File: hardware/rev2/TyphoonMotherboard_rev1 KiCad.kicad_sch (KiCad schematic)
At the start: 45 parts, among them J1 Conn_02x04_Odd_Even, J2 Conn_01x04_Pin, J3 UJ20-C-H-C-4-SMT-TR, J5 Conn_01x02_Pin, J6 Conn_01x02_Pin, J7 Conn_01x04_Pin, SW1 SW_Push, SW2 SW_Push, SW3 SW_Push, U1 USBLC6-2SC6, U2 ESP32-S3-WROOM-1, U3 SN65HVD233, U4 TPS62130A, U5 TPS62130A

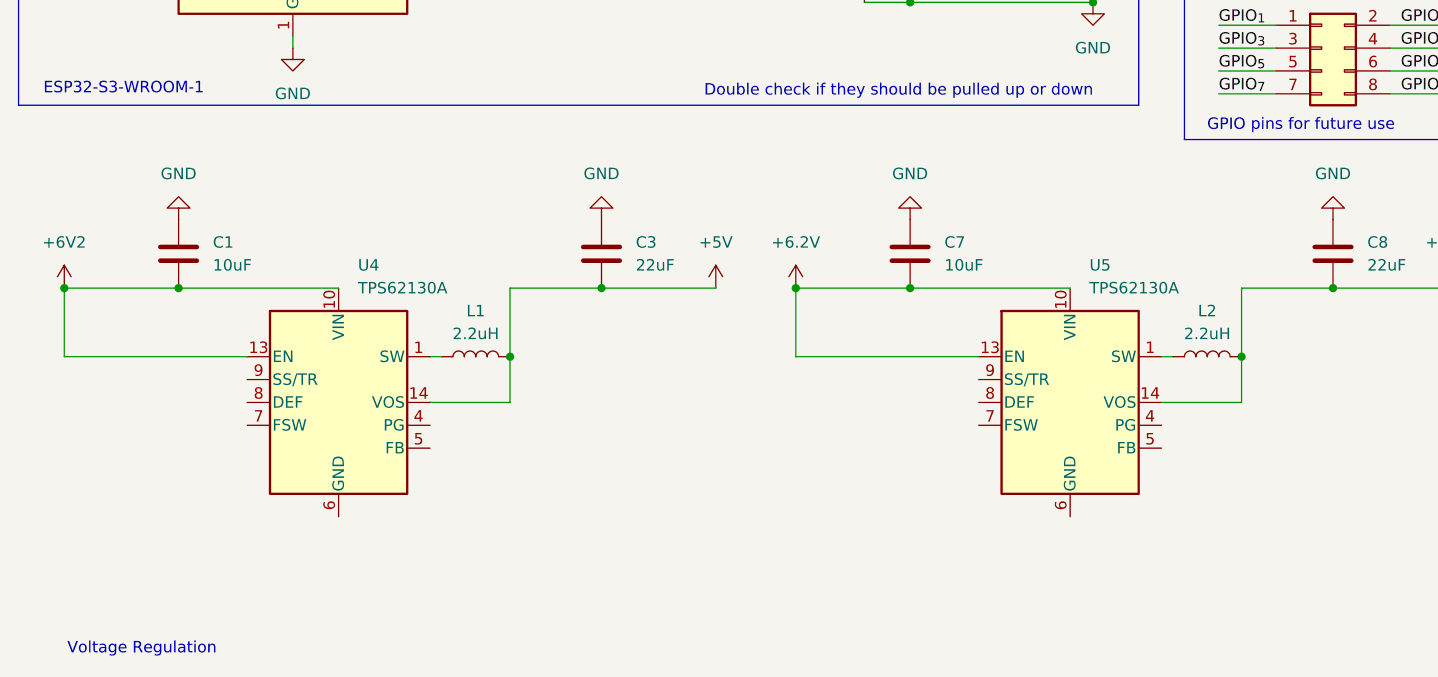
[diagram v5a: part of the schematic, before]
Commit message: Updated rev2 voltage regulation schematic (TP62133 regulator)
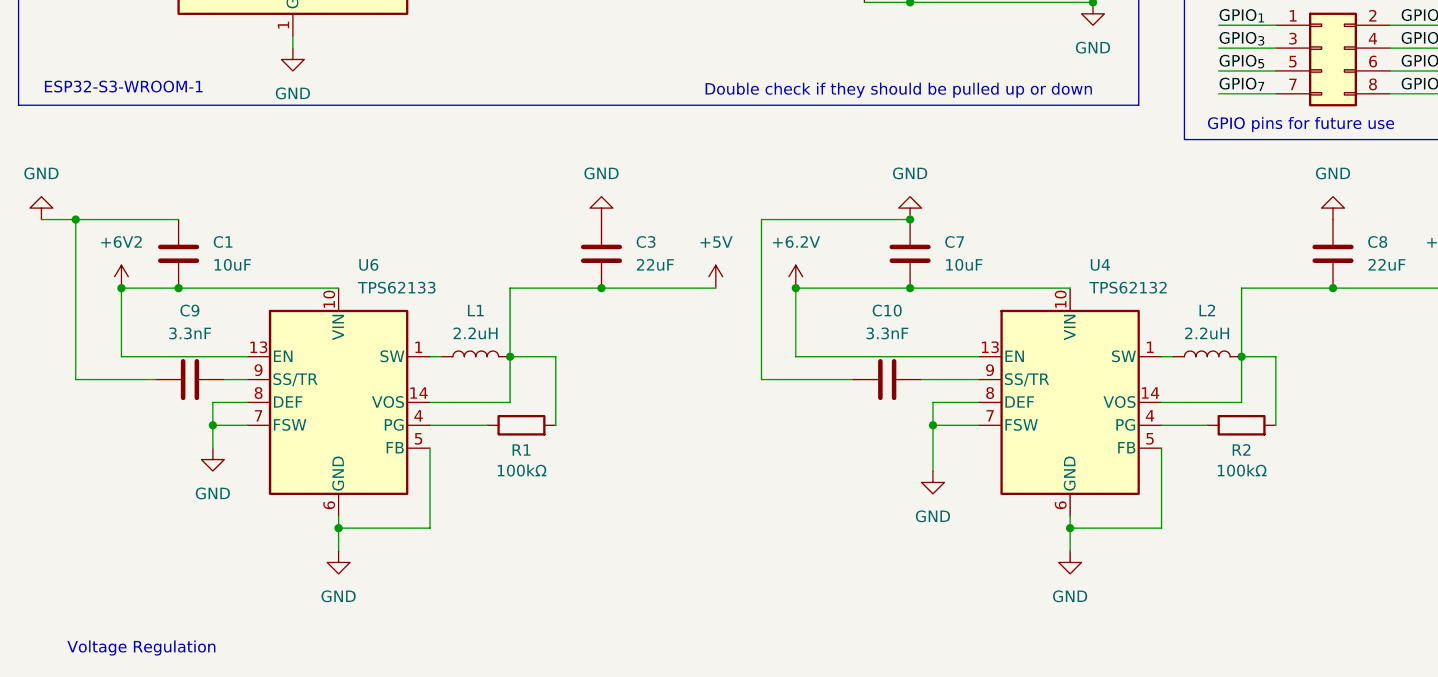
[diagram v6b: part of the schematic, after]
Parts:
- removed U4, U5: TPS62130A, Package_DFN_QFN:VQFN-16-1EP_3x3mm_P0.5mm_EP1.68x1.68mm_ThermalVias, symbol Regulator_Switching:TPS62130A
- added C10, C9: 3.3nF, symbol Device:C
- added R1, R2: 100kΩ, symbol Device:R
- added U4: TPS62132, Package_DFN_QFN:VQFN-16-1EP_3x3mm_P0.5mm_EP1.68x1.68mm_ThermalVias, symbol Regulator_Switching:TPS62132
- added U6: TPS62133, Package_DFN_QFN:VQFN-16-1EP_3x3mm_P0.5mm_EP1.68x1.68mm_ThermalVias, symbol Regulator_Switching:TPS62133
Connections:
- net +3V3: now also R2.2, U4.14 (VOS)
- net +5V: now also R1.2, U6.14 (VOS)
- net +6.2V: now also U4.10 (VIN), U4.11 (VIN), U4.12 (VIN), U4.13 (EN)
- net +6V2: now also U6.10 (VIN), U6.11 (VIN), U6.12 (VIN), U6.13 (EN)
- net GND: now also C10.1, C9.1, U4.15 (GND), U4.16 (GND), U4.17 (GND), U4.5 (FB), U4.6 (GND), U4.7 (FSW), U4.8 (DEF), U6.15 (GND), U6.16 (GND), U6.17 (GND), U6.5 (FB), U6.6 (GND), U6.7 (FSW), U6.8 (DEF)
- net at L1.1: now also U6.1 (SW), U6.2 (SW), U6.3 (SW)
- net at L2.1: now also U4.1 (SW), U4.2 (SW), U4.3 (SW)
- new net: R2.1, U4.4 (PG)
- new net: C10.2, U4.9 (SS/TR)
- new net: R1.1, U6.4 (PG)
- new net: C9.2, U6.9 (SS/TR)

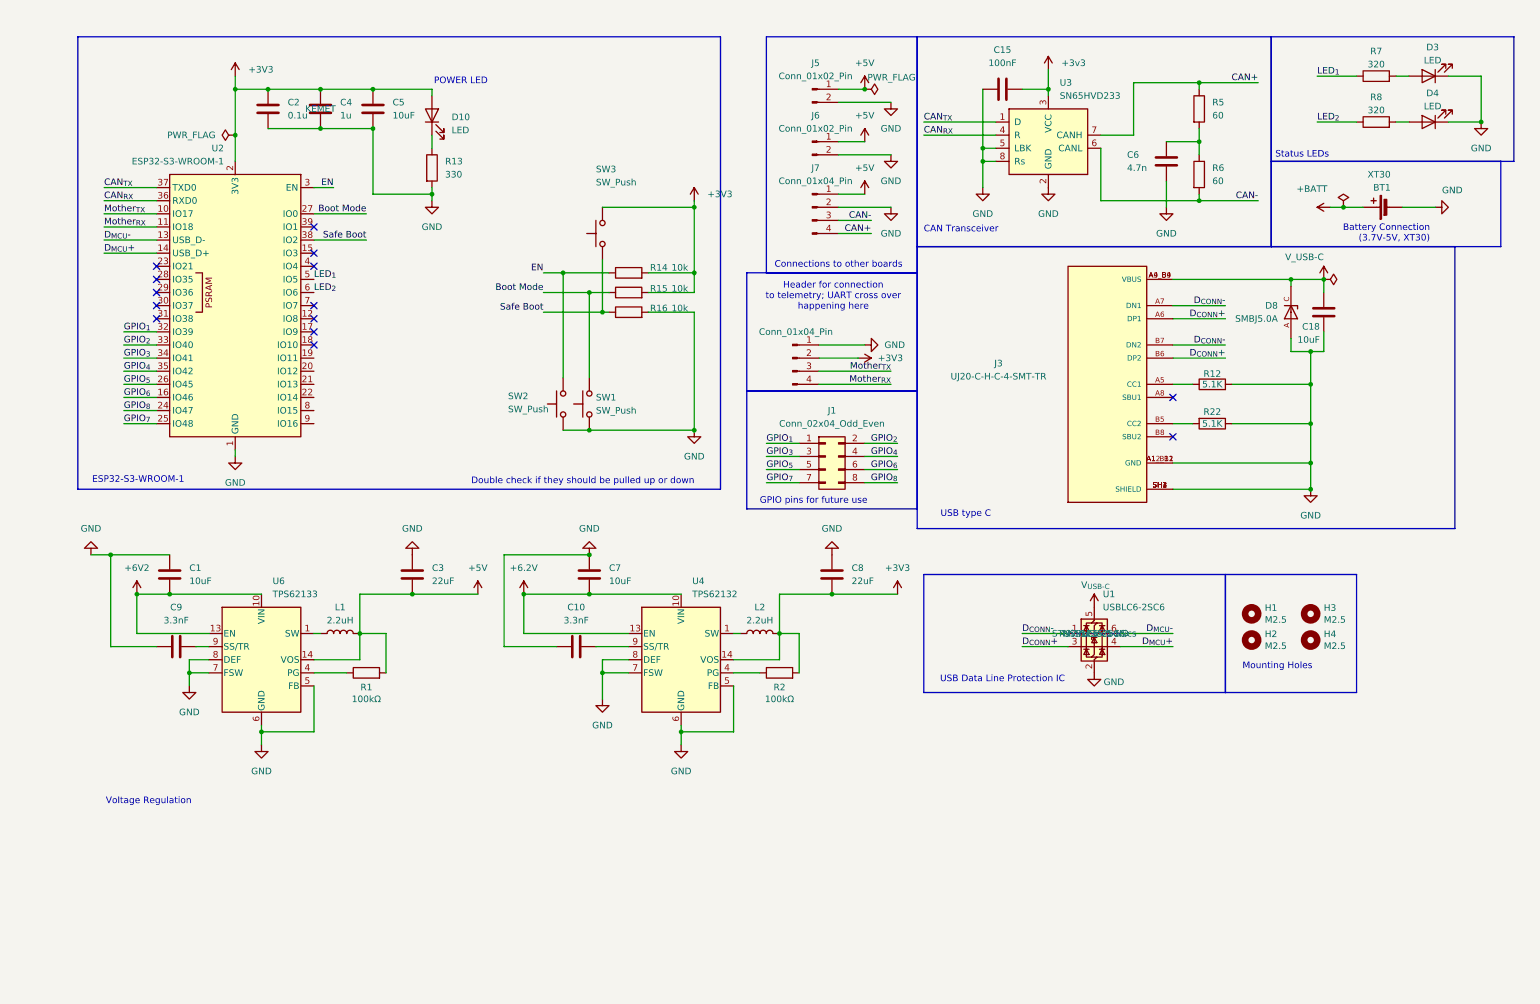
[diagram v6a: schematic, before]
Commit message: Finished Schematic Ready for PCB Design
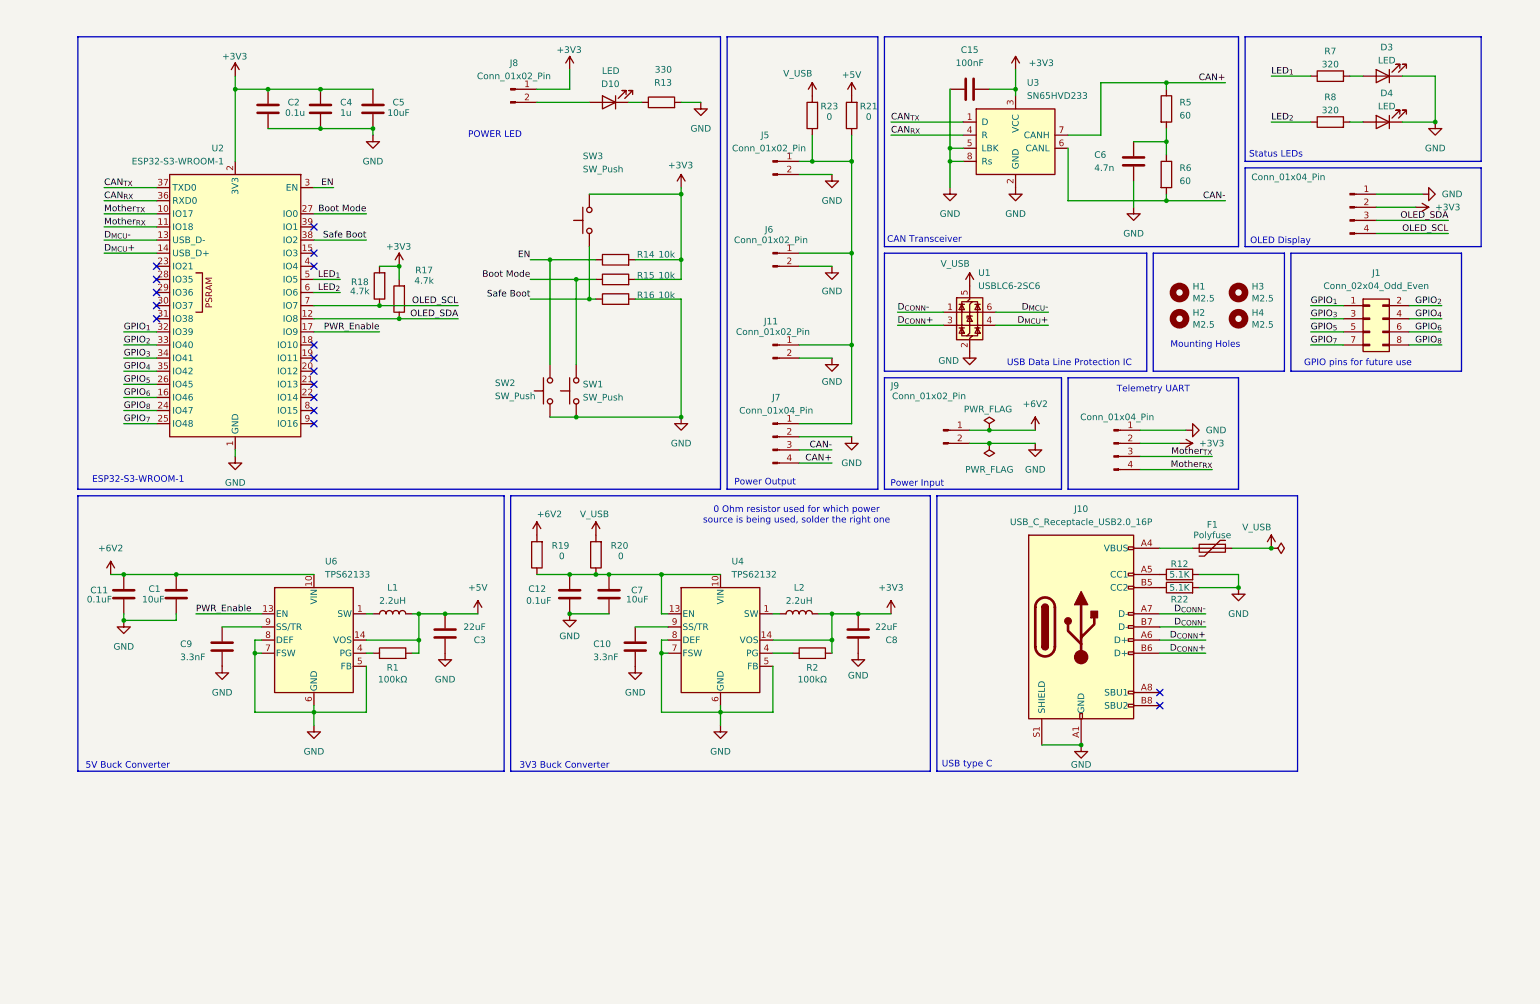
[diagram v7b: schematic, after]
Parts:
- removed BT1: XT30, Connector_AMASS:AMASS_XT30U-F_1x02_P5.0mm_Vertical, symbol Device:Battery_Cell
- removed C18: 10uF, Capacitor_SMD:C_0603_1608Metric, symbol Device:C
- removed D8: SMBJ5.0A, SMBJ5.0A:DIOM4336X265N, symbol SMBJ5.0A:SMBJ5.0A
- removed J3: UJ20-C-H-C-4-SMT-TR, UJ20-C-H-C-4-SMT-TR:CUI_UJ20-C-H-C-4-SMT-TR, symbol UJ20-C-H-C-4-SMT-TR:UJ20-C-H-C-4-SMT-TR
- added C11, C12: 0.1uF, Capacitor_SMD:C_0603_1608Metric, symbol Device:C
- added F1: Polyfuse, Fuse:Fuse_1206_3216Metric, symbol Device:Polyfuse
- added J10: USB_C_Receptacle_USB2.0_16P, Connector_USB:USB_C_Receptacle_JAE_DX07S016JA1R1500, symbol Connector:USB_C_Receptacle_USB2.0_16P
- added J11, J8, J9: Conn_01x02_Pin, Connector_JST:JST_XH_B2B-XH-A_1x02_P2.50mm_Vertical, symbol Connector:Conn_01x02_Pin
- added J4: Conn_01x04_Pin, Connector_JST:JST_XH_B4B-XH-A_1x04_P2.50mm_Vertical, symbol Connector:Conn_01x04_Pin
- added R17, R18: 4.7k, Resistor_SMD:R_0603_1608Metric, symbol Device:R
- added R19, R20, R21, R23: 0, Resistor_SMD:R_1206_3216Metric, symbol Device:R
- C1, C10, C3, C7, C8, C9: footprint (none) -> Capacitor_SMD:C_0603_1608Metric
- L1, L2: footprint (none) -> Inductor_SMD:L_0805_2012Metric
- R1, R2: footprint (none) -> Resistor_SMD:R_0603_1608Metric
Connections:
- net +3v3 is gone; now on net +3V3: C15.2, U3.3 (VCC)
- net +3V3: now also J4.2 (Pin_2), J8.1 (Pin_1), R17.2, R18.2; no longer D10.2 (A)
- net +5V: now also R21.2; no longer C3.2, J5.1 (Pin_1), J6.1 (Pin_1), J7.1 (Pin_1), L1.2, R1.2, U6.14 (VOS)
- net +6V2: now also C11.2, J9.1 (Pin_1), R19.2; no longer U6.13 (EN)
- net D_{CONN}+: now also J10.A6 (D+), J10.B6 (D+)
- net D_{CONN}-: now also J10.A7 (D-), J10.B7 (D-)
- net GND: now also R22.2, C11.1, C12.1, J10.A1 (GND), J10.A12 (GND), J10.B1 (GND), J10.B12 (GND), J10.S1 (SHIELD), J11.2 (Pin_2), J4.1 (Pin_1), J9.2 (Pin_2); no longer R22.1
- net at R12.1: now also J10.A5 (CC1)
- net OLED_SDA: now reaches U2.12 (IO8)
- net OLED_SDA: now also J4.3 (Pin_3), R17.1
- net PWR_Enable: now reaches U2.17 (IO9)
- net PWR_Enable: now also U6.13 (EN)
- net OLED_SCL: now reaches U2.7 (IO7)
- net OLED_SCL: now also J4.4 (Pin_4), R18.1
- net +6.2V: no longer names the net of C7.2, U4.10 (VIN), U4.11 (VIN), U4.12 (VIN), U4.13 (EN)
- net +6.2V: now also C12.2, R19.1, R20.1
- net V_{USB-C} renamed V_USB
- net V_USB: now also F1.1, R20.2, R23.2
- new net: D10.2 (A), J8.2 (Pin_2)
- new net: C3.2, L1.2, R1.2, U6.14 (VOS)
- new net: J10.B5 (CC2), R22.1
- new net: F1.2, J10.A4 (VBUS), J10.A9 (VBUS), J10.B4 (VBUS), J10.B9 (VBUS)
- new net: J11.1 (Pin_1), J5.1 (Pin_1), J6.1 (Pin_1), J7.1 (Pin_1), R21.1, R23.1
- no-connect marks 14 -> 17
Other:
- note added: "0 Ohm resistor used for which power source is being used, solder the right one"
- note added: "3V3 Buck Converter"
- note added: "5V Buck Converter"
- note added: "OLED Display"
- note added: "Power Input"
- note added: "Power Output"
- note added: "Telemetry UART"
- note removed: "Battery Connection (3.7V-5V, XT30)"
- note removed: "Connections to other boards"
- note removed: "Double check if they should be pulled up or down"
- note removed: "Header for connection to telemetry; UART cross over happening here"
- note removed: "Voltage Regulation"
- moved on the sheet: C1, C15, C3, C6, C7, C8, C9, D10, D3, D4, H1, H2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

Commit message: <UPDATE> Oliver Review Ver
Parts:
- removed R16: 10k, Resistor_SMD:R_0603_1608Metric, symbol Device:R
- removed SW3: SW_Push, Connector_PinHeader_2.54mm:PinHeader_1x02_P2.54mm_Vertical, symbol Switch:SW_Push
- J8: footprint Connector_JST:JST_XH_B2B-XH-A_1x02_P2.50mm_Vertical -> Connector_PinHeader_2.54mm:PinHeader_1x02_P2.54mm_Vertical
- SW1, SW2: footprint Connector_PinHeader_2.54mm:PinHeader_1x02_P2.54mm_Vertical -> (none)
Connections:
- net +5V: now also C3.2, L1.2, R1.2, U6.14 (VOS)
- net GPIO_{1}: now also U2.28 (IO35); no longer U2.32 (IO39)
- net GPIO_{2}: now also U2.29 (IO36); no longer U2.33 (IO40)
- net GPIO_{3}: now also U2.30 (IO37); no longer U2.34 (IO41)
- net GPIO_{4}: now also U2.31 (IO38); no longer U2.35 (IO42)
- net GPIO_{5}: now also U2.32 (IO39); no longer U2.26 (IO45)
- net GPIO_{6}: now also U2.33 (IO40); no longer U2.16 (IO46)
- net GPIO_{7}: now also U2.34 (IO41); no longer U2.25 (IO48)
- net GPIO_{8}: now also U2.35 (IO42); no longer U2.24 (IO47)
- net LED_{1}: now also U2.4 (IO4); no longer U2.5 (IO5)
- net LED_{2}: now also U2.5 (IO5); no longer U2.6 (IO6)
- net Mother_{RX}: now also J2.3 (Pin_3); no longer J2.4 (Pin_4)
- net Mother_{TX}: now also J2.4 (Pin_4); no longer J2.3 (Pin_3)
- net OLED_SCL: now also R17.1, U2.6 (IO6); no longer R18.1, U2.7 (IO7)
- net OLED_SDA: now also R18.1, U2.7 (IO7); no longer R17.1, U2.12 (IO8)
- net PWR_Enable: now also U2.26 (IO45); no longer U2.17 (IO9)
- net Safe Boot: no longer names the net of U2.38 (IO2)
- no-connect marks 17 -> 18
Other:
- moved on the sheet: C2, C4, C5, R14, R15, SW1, SW2, U2
